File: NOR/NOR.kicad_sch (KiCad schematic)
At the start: 2 parts, among them J1 5-146280-3-ND, J2 5-146280-3-ND

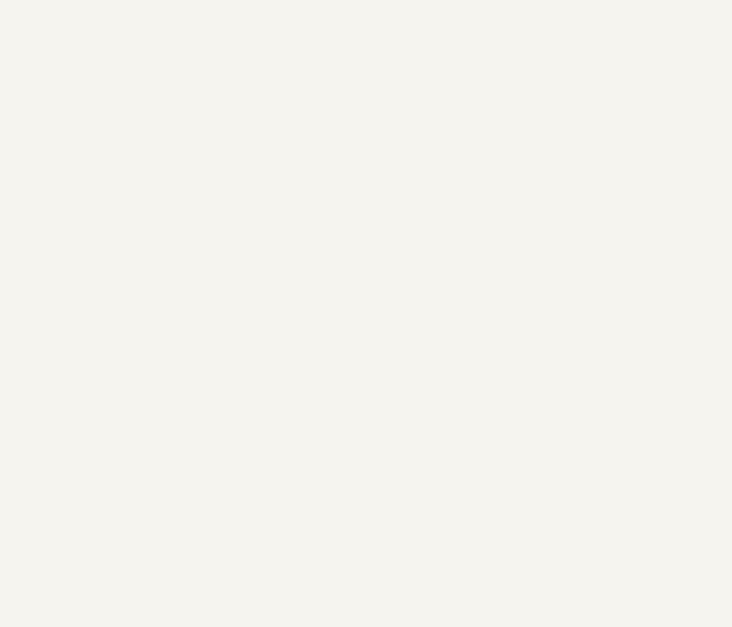
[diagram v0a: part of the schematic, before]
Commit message: Finish NOR gate PCB and unify NAND with it
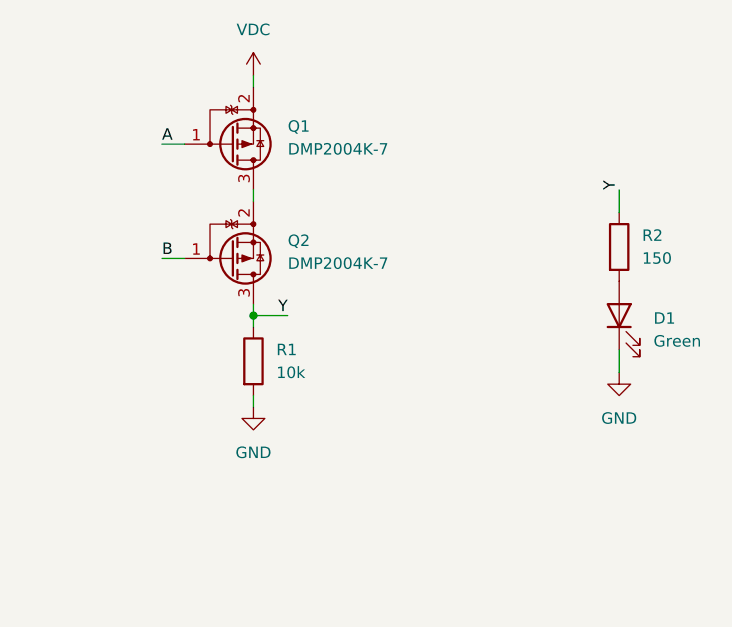
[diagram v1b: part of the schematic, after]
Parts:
- added D1: Green, LED_SMD:LED_0603_1608Metric, symbol Device:LED
- added Q1, Q2: DMP2004K-7, Package_TO_SOT_SMD:SOT-23, symbol Logic:DMP2004K-7
- added R1: 10k, Resistor_SMD:R_0603_1608Metric, symbol Device:R
- added R2: 150, Resistor_SMD:R_0603_1608Metric, symbol Device:R
- J2: footprint Logic:PinHeader_1x03_P2.54mm_Vertical_Top -> Logic:PinHeader_1x03_P2.54mm_Vertical_Bottom
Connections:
- net A: now also Q1.1 (G)
- net B: now also Q2.1 (G)
- net GND: now also D1.1 (K), R1.2
- net VDC: now also Q1.2 (S)
- net Y: now also Q2.3 (D), R1.1, R2.1
- new net: D1.2 (A), R2.2
- new net: Q1.3 (D), Q2.2 (S)
